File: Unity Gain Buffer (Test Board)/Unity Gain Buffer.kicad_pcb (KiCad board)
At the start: 2 copper layers, 31 x 21 mm, 3 parts, among them J1 CONN_01X04, U1 MCP601ST

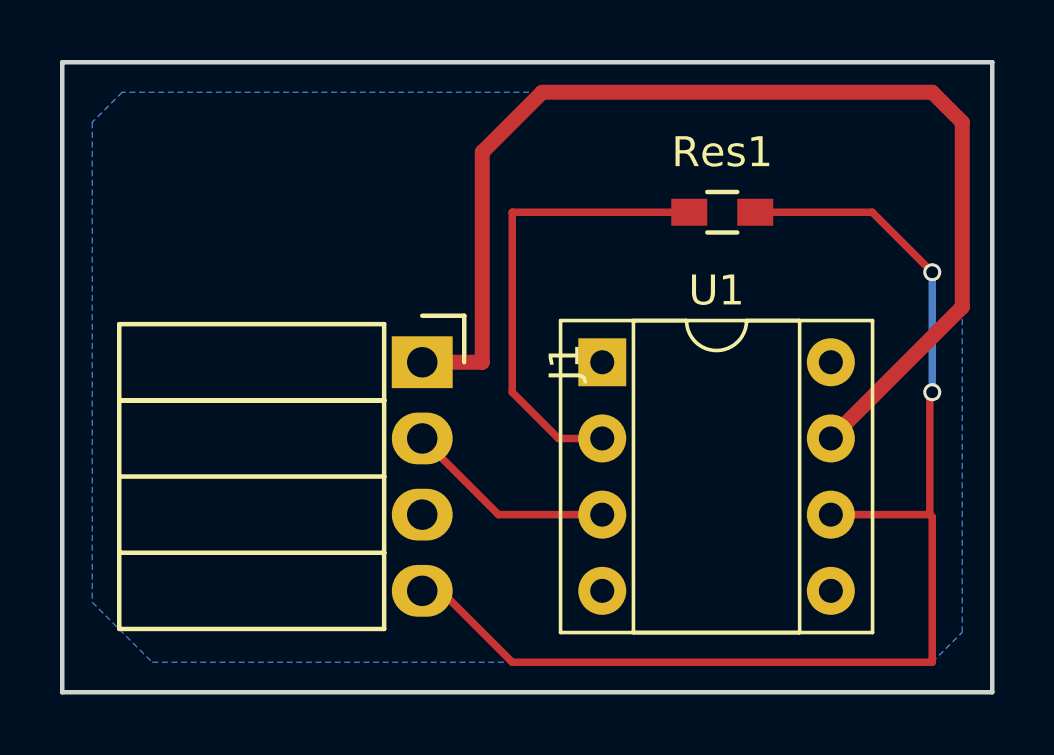
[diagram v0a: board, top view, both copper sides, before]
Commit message: updating for 79 and myDAQ boards
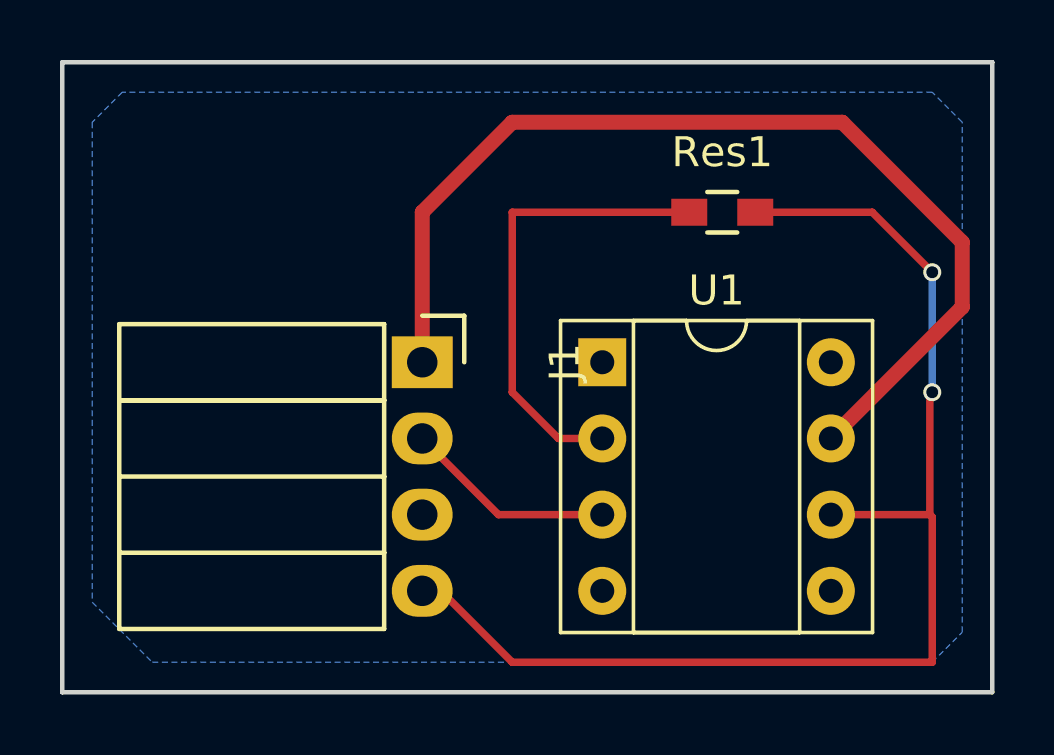
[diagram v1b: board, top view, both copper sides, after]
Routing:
- net +5V: track 38.6 -> 34.3 mm
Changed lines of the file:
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@@
     (thickness 1.6)
     (drawings 4)
-    (tracks 26)
+    (tracks 25)
     (zones 0)
     (modules 3)
@@
   (segment (start 137.54 103.08) (end 135 100.54) (width 0.25) (layer F.Cu) (net 5))
   (segment (start 141 103.08) (end 137.54 103.08) (width 0.25) (layer F.Cu) (net 5))
-  (segment (start 135 98) (end 137 98) (width 0.5) (layer F.Cu) (net 6))
+  (segment (start 135 98) (end 135 93) (width 0.5) (layer F.Cu) (net 6))
   (segment (start 153 96.16) (end 148.62 100.54) (width 0.5) (layer F.Cu) (net 6))
-  (segment (start 153 90) (end 153 96.16) (width 0.5) (layer F.Cu) (net 6))
-  (segment (start 152 89) (end 153 90) (width 0.5) (layer F.Cu) (net 6))
-  (segment (start 139 89) (end 152 89) (width 0.5) (layer F.Cu) (net 6))
-  (segment (start 137 91) (end 139 89) (width 0.5) (layer F.Cu) (net 6))
-  (segment (start 137 98) (end 137 91) (width 0.5) (layer F.Cu) (net 6))
+  (segment (start 153 94) (end 153 96.16) (width 0.5) (layer F.Cu) (net 6))
+  (segment (start 149 90) (end 153 94) (width 0.5) (layer F.Cu) (net 6))
+  (segment (start 138 90) (end 149 90) (width 0.5) (layer F.Cu) (net 6))
+  (segment (start 135 93) (end 138 90) (width 0.5) (layer F.Cu) (net 6))
   (zone (net 7) (net_name GND) (layer B.Cu) (hatch edge 0.508)
     (connect_pads (clearance 0.508))
